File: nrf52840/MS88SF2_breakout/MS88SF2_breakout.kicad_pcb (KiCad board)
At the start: 2 copper layers, 3 parts, among them J1 Conn_01x14_Male, J2 Conn_01x14_Male, U1 MS88SF2

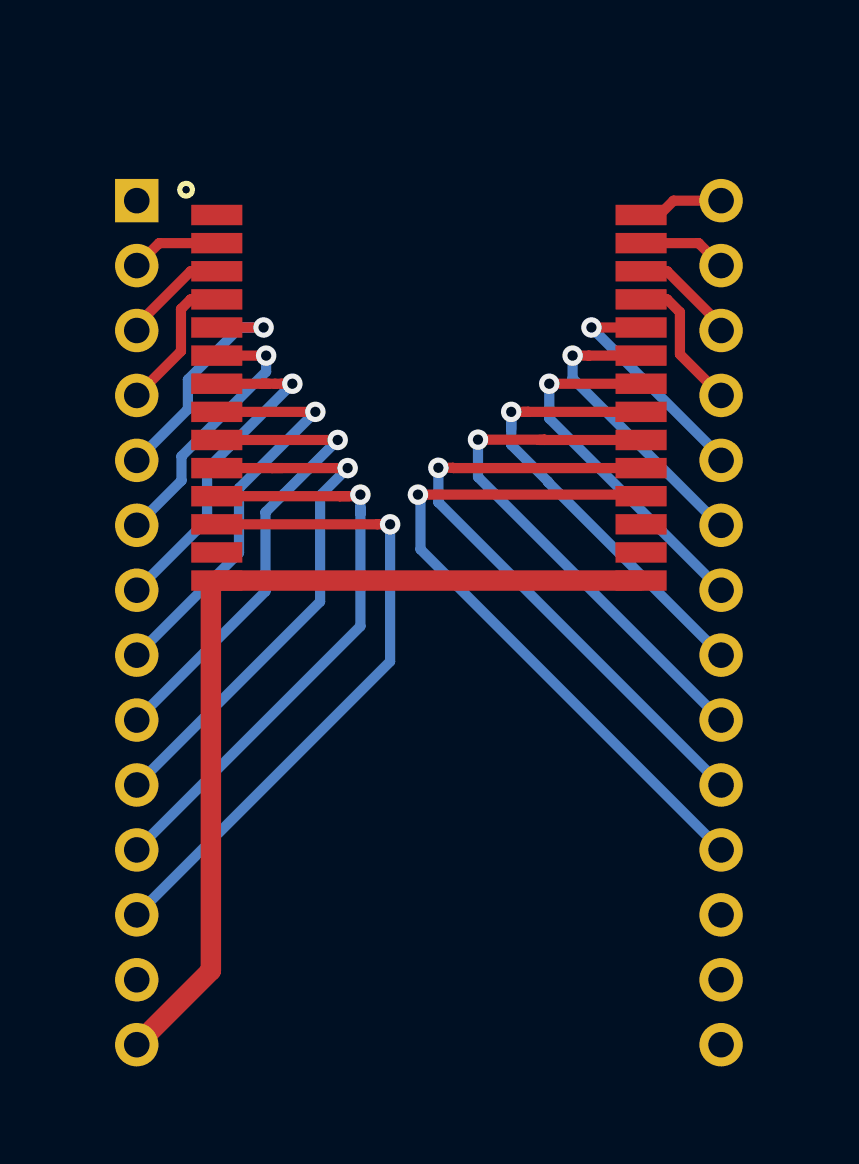
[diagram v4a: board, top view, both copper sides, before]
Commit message: nrf5: Add edge cuts
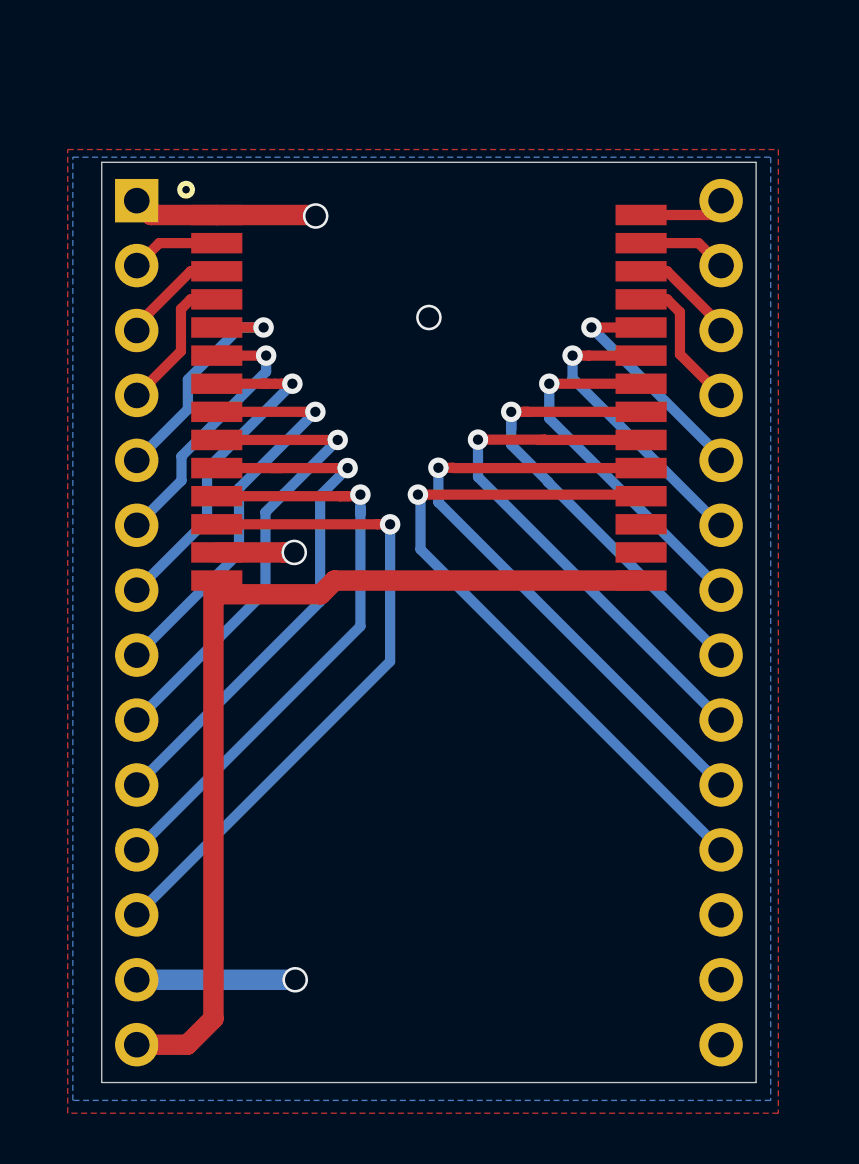
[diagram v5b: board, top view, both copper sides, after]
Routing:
- net GND: track 0.00 -> 16.5 mm, vias 0 -> 4
- net +3V3: track 36.1 -> 37.0 mm
- net P0.10: track 3.36 -> 3.91 mm
- added copper zone on B.Cu, net GND
- added copper zone on F.Cu, net GND
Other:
- board outline added: 25.6 x 36 mm
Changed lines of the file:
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@@
   (general
     (thickness 1.6)
-    (drawings 0)
-    (tracks 132)
+    (drawings 4)
+    (tracks 147)
     (zones 0)
     (modules 3)
@@
   )
   (setup
-    (last_trace_width 0.4)
+    (last_trace_width 0.8)
     (user_trace_width 0.3)
     (user_trace_width 0.4)
@@
       (effects (font (size 1 1) (thickness 0.15)))
     )
+    (fp_line (start 8.7 -11.6) (end -8.7 -11.6) (layer F.Fab) (width 0.12))
+    (fp_line (start -8.7 -11.6) (end -8.7 11.6) (layer F.Fab) (width 0.12))
+    (fp_line (start -8.7 11.6) (end 8.7 11.6) (layer F.Fab) (width 0.12))
+    (fp_line (start 8.7 11.6) (end 8.7 -11.6) (layer F.Fab) (width 0.12))
+    (fp_line (start -8.7 -5.81) (end -12.7 -5.81) (layer F.Fab) (width 0.12))
+    (fp_line (start -12.7 -5.81) (end -12.7 -17.6) (layer F.Fab) (width 0.12))
+    (fp_line (start 8.7 -5.81) (end 12.7 -5.81) (layer F.Fab) (width 0.12))
+    (fp_line (start 12.7 -5.81) (end 12.7 -17.6) (layer F.Fab) (width 0.12))
+    (fp_line (start 8.7 -5.81) (end -8.7 -5.81) (layer F.Fab) (width 0.12))
+    (fp_line (start 12.7 -17.6) (end -12.7 -17.6) (layer F.Fab) (width 0.12))
+    (fp_circle (center -9.5 -5) (end -9.4 -5) (layer F.SilkS) (width 0.5))
+    (fp_line (start 12.7 -5.81) (end -12.7 -17.6) (layer F.Fab) (width 0.12))
     (fp_line (start -12.7 -5.81) (end 12.7 -17.6) (layer F.Fab) (width 0.12))
-    (fp_line (start 12.7 -5.81) (end -12.7 -17.6) (layer F.Fab) (width 0.12))
-    (fp_circle (center -9.5 -5) (end -9.4 -5) (layer F.SilkS) (width 0.5))
-    (fp_line (start 12.7 -17.6) (end -12.7 -17.6) (layer F.Fab) (width 0.12))
-    (fp_line (start 8.7 -5.81) (end -8.7 -5.81) (layer F.Fab) (width 0.12))
-    (fp_line (start 12.7 -5.81) (end 12.7 -17.6) (layer F.Fab) (width 0.12))
-    (fp_line (start 8.7 -5.81) (end 12.7 -5.81) (layer F.Fab) (width 0.12))
-    (fp_line (start -12.7 -5.81) (end -12.7 -17.6) (layer F.Fab) (width 0.12))
-    (fp_line (start -8.7 -5.81) (end -12.7 -5.81) (layer F.Fab) (width 0.12))
-    (fp_line (start 8.7 11.6) (end 8.7 -11.6) (layer F.Fab) (width 0.12))
-    (fp_line (start -8.7 11.6) (end 8.7 11.6) (layer F.Fab) (width 0.12))
-    (fp_line (start -8.7 -11.6) (end -8.7 11.6) (layer F.Fab) (width 0.12))
-    (fp_line (start 8.7 -11.6) (end -8.7 -11.6) (layer F.Fab) (width 0.12))
     (fp_text user "No copper" (at 0 -16) (layer F.Fab)
       (effects (font (size 1 1) (thickness 0.15)))
@@
       (effects (font (size 1 1) (thickness 0.15)))
     )
+    (fp_line (start -0.635 -1.27) (end 1.27 -1.27) (layer F.Fab) (width 0.1))
+    (fp_line (start 1.27 -1.27) (end 1.27 34.29) (layer F.Fab) (width 0.1))
+    (fp_line (start 1.27 34.29) (end -1.27 34.29) (layer F.Fab) (width 0.1))
+    (fp_line (start -1.27 34.29) (end -1.27 -0.635) (layer F.Fab) (width 0.1))
     (fp_line (start -1.27 -0.635) (end -0.635 -1.27) (layer F.Fab) (width 0.1))
-    (fp_line (start -1.27 34.29) (end -1.27 -0.635) (layer F.Fab) (width 0.1))
-    (fp_line (start 1.27 34.29) (end -1.27 34.29) (layer F.Fab) (width 0.1))
-    (fp_line (start 1.27 -1.27) (end 1.27 34.29) (layer F.Fab) (width 0.1))
-    (fp_line (start -0.635 -1.27) (end 1.27 -1.27) (layer F.Fab) (width 0.1))
     (fp_text user %R (at 0 16.51 90) (layer F.Fab)
       (effects (font (size 1 1) (thickness 0.15)))
@@
       (effects (font (size 1 1) (thickness 0.15)))
     )
+    (fp_line (start -1.27 -0.635) (end -0.635 -1.27) (layer F.Fab) (width 0.1))
+    (fp_line (start -1.27 34.29) (end -1.27 -0.635) (layer F.Fab) (width 0.1))
+    (fp_line (start 1.27 34.29) (end -1.27 34.29) (layer F.Fab) (width 0.1))
+    (fp_line (start 1.27 -1.27) (end 1.27 34.29) (layer F.Fab) (width 0.1))
     (fp_line (start -0.635 -1.27) (end 1.27 -1.27) (layer F.Fab) (width 0.1))
-    (fp_line (start 1.27 -1.27) (end 1.27 34.29) (layer F.Fab) (width 0.1))
-    (fp_line (start 1.27 34.29) (end -1.27 34.29) (layer F.Fab) (width 0.1))
-    (fp_line (start -1.27 34.29) (end -1.27 -0.635) (layer F.Fab) (width 0.1))
-    (fp_line (start -1.27 -0.635) (end -0.635 -1.27) (layer F.Fab) (width 0.1))
     (fp_text user %R (at 0 16.51 90) (layer F.Fab)
       (effects (font (size 1 1) (thickness 0.15)))
@@
     )
   )
-  (segment (start 66.13 74.862) (end 82.73 74.862) (width 0.8) (layer F.Cu) (net 1))
-  (segment (start 65.9 75.092) (end 66.13 74.862) (width 0.8) (layer F.Cu) (net 1))
-  (segment (start 65.9 90.12) (end 65.9 75.092) (width 0.8) (layer F.Cu) (net 1))
-  (segment (start 63 93.02) (end 65.9 90.12) (width 0.8) (layer F.Cu) (net 1))
+  (gr_line (start 87.23 94.5) (end 61.63 94.5) (layer Edge.Cuts) (width 0.05))
+  (gr_line (start 87.23 58.5) (end 61.63 58.5) (layer Edge.Cuts) (width 0.05))
+  (gr_line (start 87.23 58.5) (end 87.23 94.5) (layer Edge.Cuts) (width 0.05))
+  (gr_line (start 61.63 58.5) (end 61.63 94.5) (layer Edge.Cuts) (width 0.05))
+  (segment (start 64.98 93.02) (end 63 93.02) (width 0.8) (layer F.Cu) (net 1))
+  (segment (start 64.98 93.02) (end 66 92) (width 0.8) (layer F.Cu) (net 1))
+  (segment (start 66 92) (end 66 75) (width 0.8) (layer F.Cu) (net 1))
+  (segment (start 82.73 74.862) (end 70.738 74.862) (width 0.8) (layer F.Cu) (net 1))
+  (segment (start 70.738 74.862) (end 70.2 75.4) (width 0.8) (layer F.Cu) (net 1))
+  (segment (start 70.2 75.4) (end 66.4 75.4) (width 0.8) (layer F.Cu) (net 1))
+  (segment (start 66.13 73.762) (end 68.762 73.762) (width 0.8) (layer F.Cu) (net 2))
+  (segment (start 69.162 73.762) (end 69.162 73.762) (width 0.8) (layer F.Cu) (net 2))
+  (segment (start 69.162 73.762) (end 68.762 73.762) (width 0.8) (layer F.Cu) (net 2))
+  (via (at 69.162 73.762) (size 1) (drill 0.8) (layers F.Cu B.Cu) (net 2))
+  (segment (start 63.562 60.562) (end 63 60) (width 0.8) (layer F.Cu) (net 2))
+  (segment (start 66.13 60.562) (end 63.562 60.562) (width 0.8) (layer F.Cu) (net 2))
+  (segment (start 63 90.48) (end 69.2 90.48) (width 0.8) (layer B.Cu) (net 2))
+  (segment (start 69.2 90.48) (end 69.2 90.48) (width 0.8) (layer B.Cu) (net 2))
+  (via (at 69.2 90.48) (size 1) (drill 0.8) (layers F.Cu B.Cu) (net 2))
+  (via (at 74.43 64.572) (size 1) (drill 0.8) (layers F.Cu B.Cu) (net 2))
+  (via (at 70 60.6) (size 1) (drill 0.8) (layers F.Cu B.Cu) (net 2))
+  (segment (start 69.962 60.562) (end 70 60.6) (width 0.8) (layer F.Cu) (net 2))
+  (segment (start 66.13 60.562) (end 69.962 60.562) (width 0.8) (layer F.Cu) (net 2))
   (segment (start 82.73 60.562) (end 83.438 60.562) (width 0.4) (layer F.Cu) (net 3))
-  (segment (start 84 60) (end 85.86 60) (width 0.4) (layer F.Cu) (net 3))
-  (segment (start 83.438 60.562) (end 84 60) (width 0.4) (layer F.Cu) (net 3))
+  (segment (start 85.69801 60.562) (end 85.86 60.40001) (width 0.4) (layer F.Cu) (net 3))
+  (segment (start 82.73 60.562) (end 85.69801 60.562) (width 0.4) (layer F.Cu) (net 3))
   (segment (start 84.982 61.662) (end 85.86 62.54) (width 0.4) (layer F.Cu) (net 4))
   (segment (start 82.73 61.662) (end 84.982 61.662) (width 0.4) (layer F.Cu) (net 4))
@@
   (segment (start 63.878 61.662) (end 63 62.54) (width 0.4) (layer F.Cu) (net 24))
   (segment (start 66.13 61.662) (end 63.878 61.662) (width 0.4) (layer F.Cu) (net 24))
+  (zone (net 2) (net_name GND) (layer B.Cu) (hatch edge 0.508)
+    (connect_pads (clearance 0.508))
+    (min_thickness 0.254)
+    (fill yes (arc_segments 32) (thermal_gap 0.508) (thermal_bridge_width 0.508))
+    (polygon
+      (pts
+        (xy 87.8 95.2) (xy 60.5 95.2) (xy 60.5 58.3) (xy 87.8 58.3)
+      )
+    )
+  )
+  (zone (net 2) (net_name GND) (layer F.Cu) (hatch edge 0.508)
+    (connect_pads (clearance 0.508))
+    (min_thickness 0.254)
+    (fill yes (arc_segments 32) (thermal_gap 0.508) (thermal_bridge_width 0.508))
+    (polygon
+      (pts
+        (xy 88.1 95.7) (xy 60.3 95.7) (xy 60.3 58) (xy 88.1 58)
+      )
+    )
+  )
+  (zone (net 0) (net_name "") (layers F&B.Cu) (hatch edge 0.508)
+    (connect_pads (clearance 0.508))
+    (min_thickness 0.254)
+    (keepout (tracks allowed) (vias allowed) (copperpour not_allowed))
+    (fill (arc_segments 32) (thermal_gap 0.508) (thermal_bridge_width 0.508))
+    (polygon
+      (pts
+        (xy 87.39986 60) (xy 60.60014 60) (xy 60.7 46.8) (xy 61.4 46.8) (xy 87.5 46.6)
+      )
+    )
+  )
 )
